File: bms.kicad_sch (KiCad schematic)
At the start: 101 parts, among them J1 CELL_TAPS, J2 SWD, J3 I2C_IN, J4 I2C_OUT, SW1 SW_Push, U1 LMR51610, U2 STM32F103C8Tx, U3 MAX14920, U4 MAX11163, U5 MAX6126, U6 ADuM1252, Y1 8M

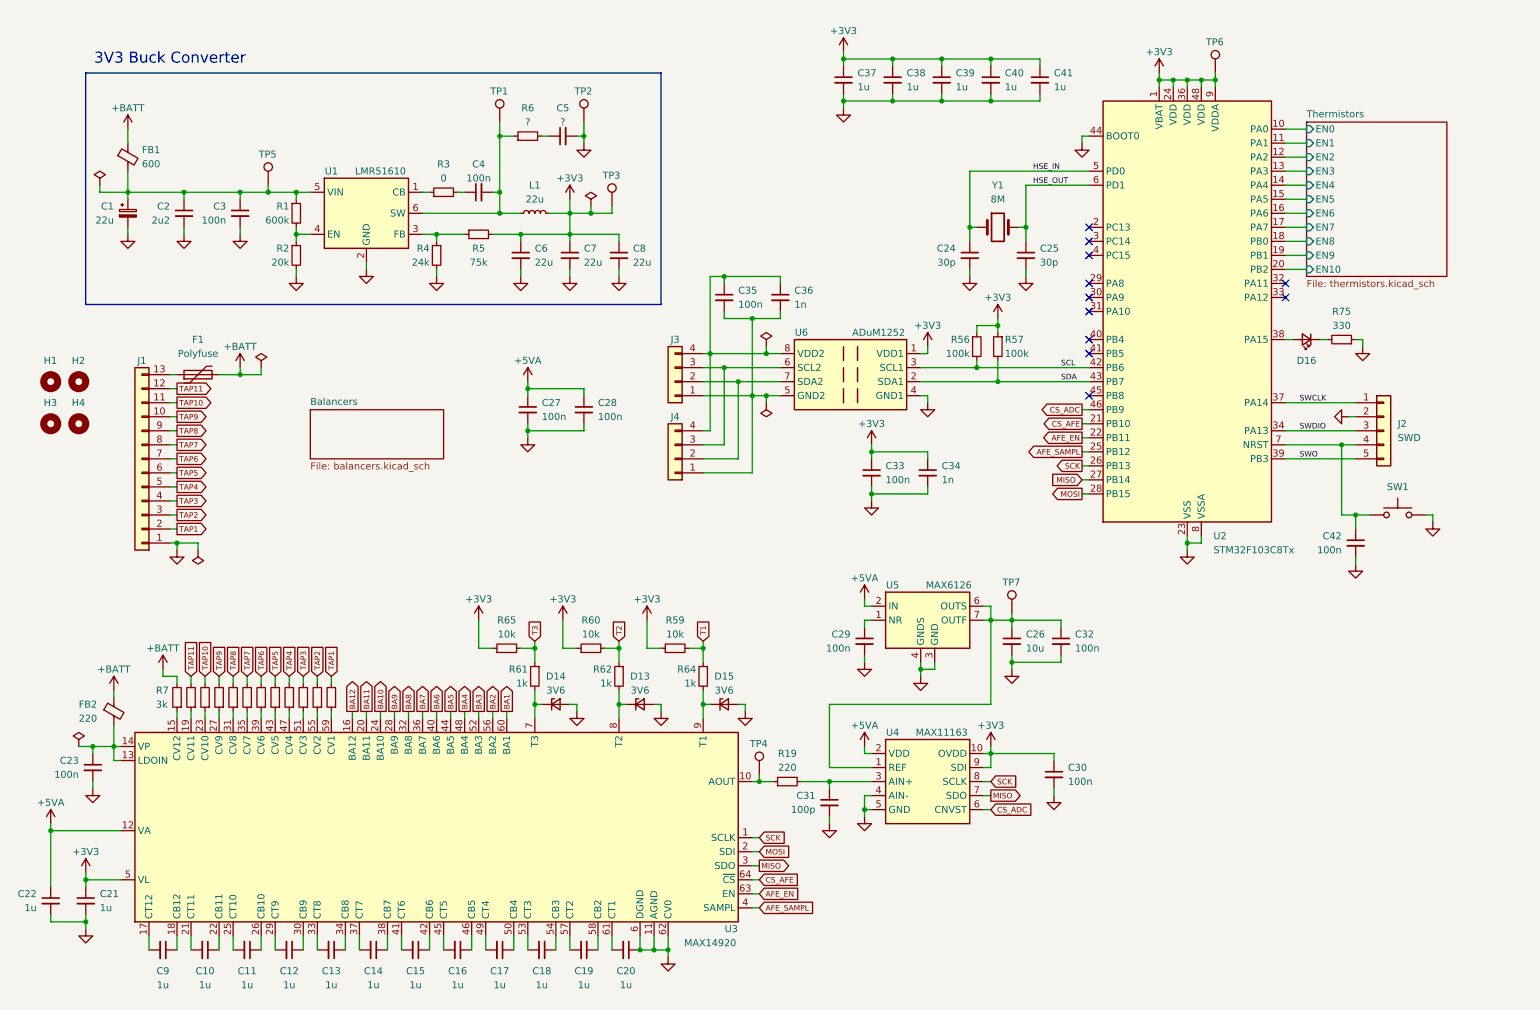
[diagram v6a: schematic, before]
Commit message: schematic: Cleanup
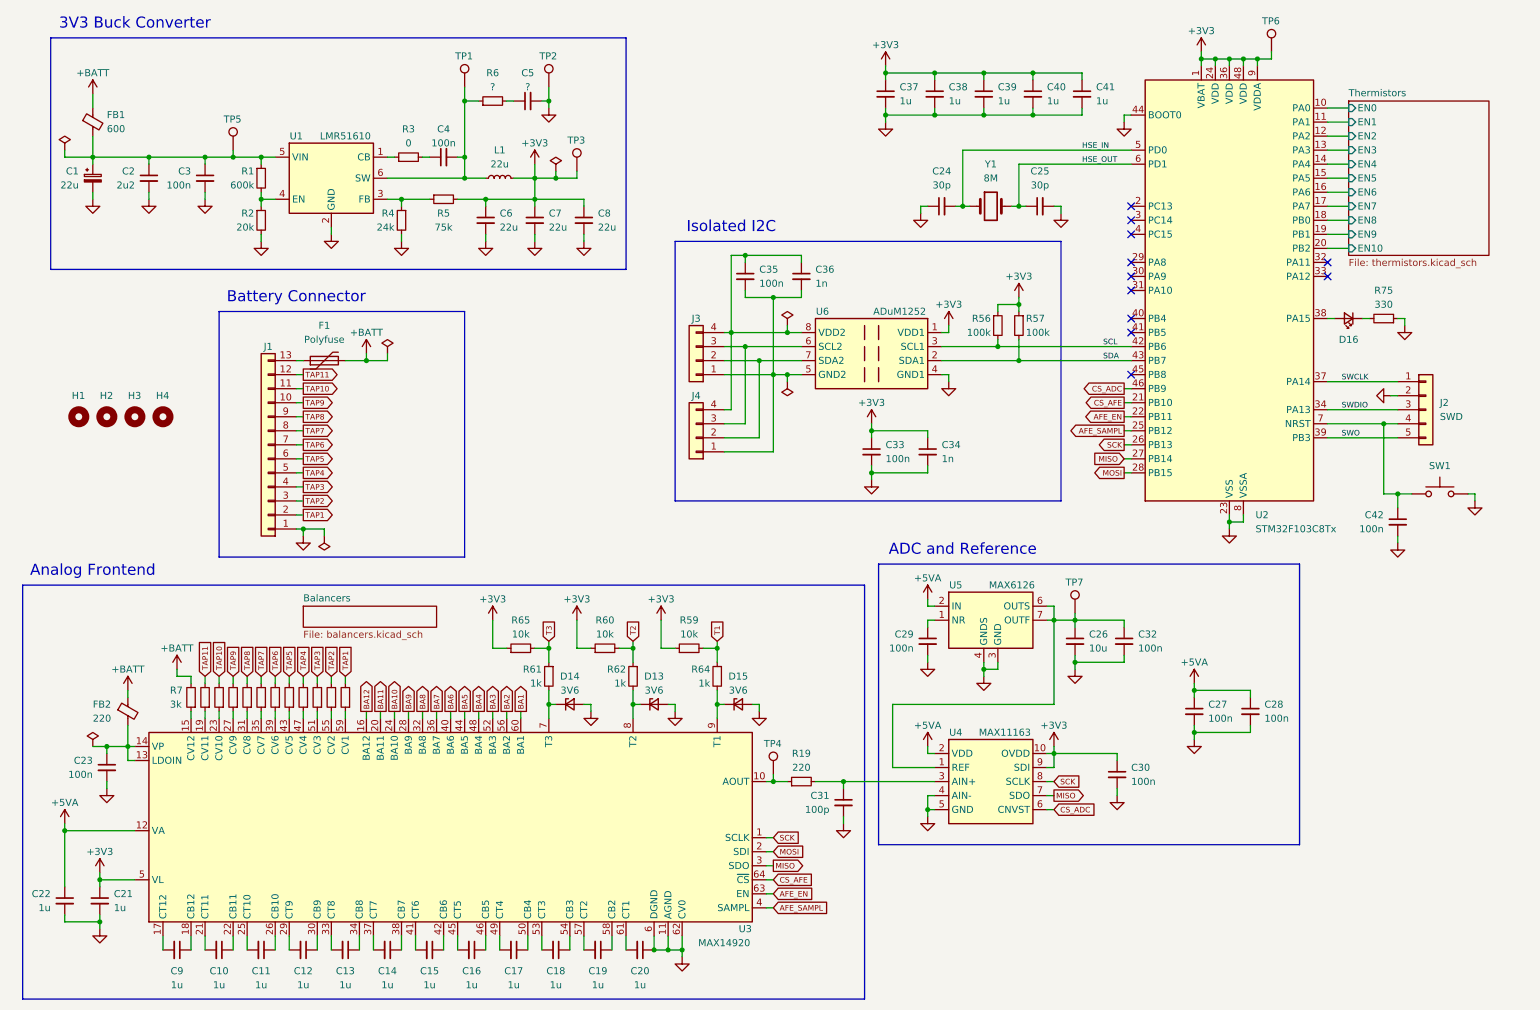
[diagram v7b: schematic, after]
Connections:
- net GND: now also C24.1; no longer C24.2
- net HSE_IN: now also C24.2; no longer C24.1
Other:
- note added: "ADC and Reference"
- note added: "Analog Frontend"
- note added: "Battery Connector"
- note added: "Isolated I2C"
- moved on the sheet: C1, C10, C11, C12, C13, C14, C15, C16, C17, C18, C19, C2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

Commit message: schematic: Re-annotate designators
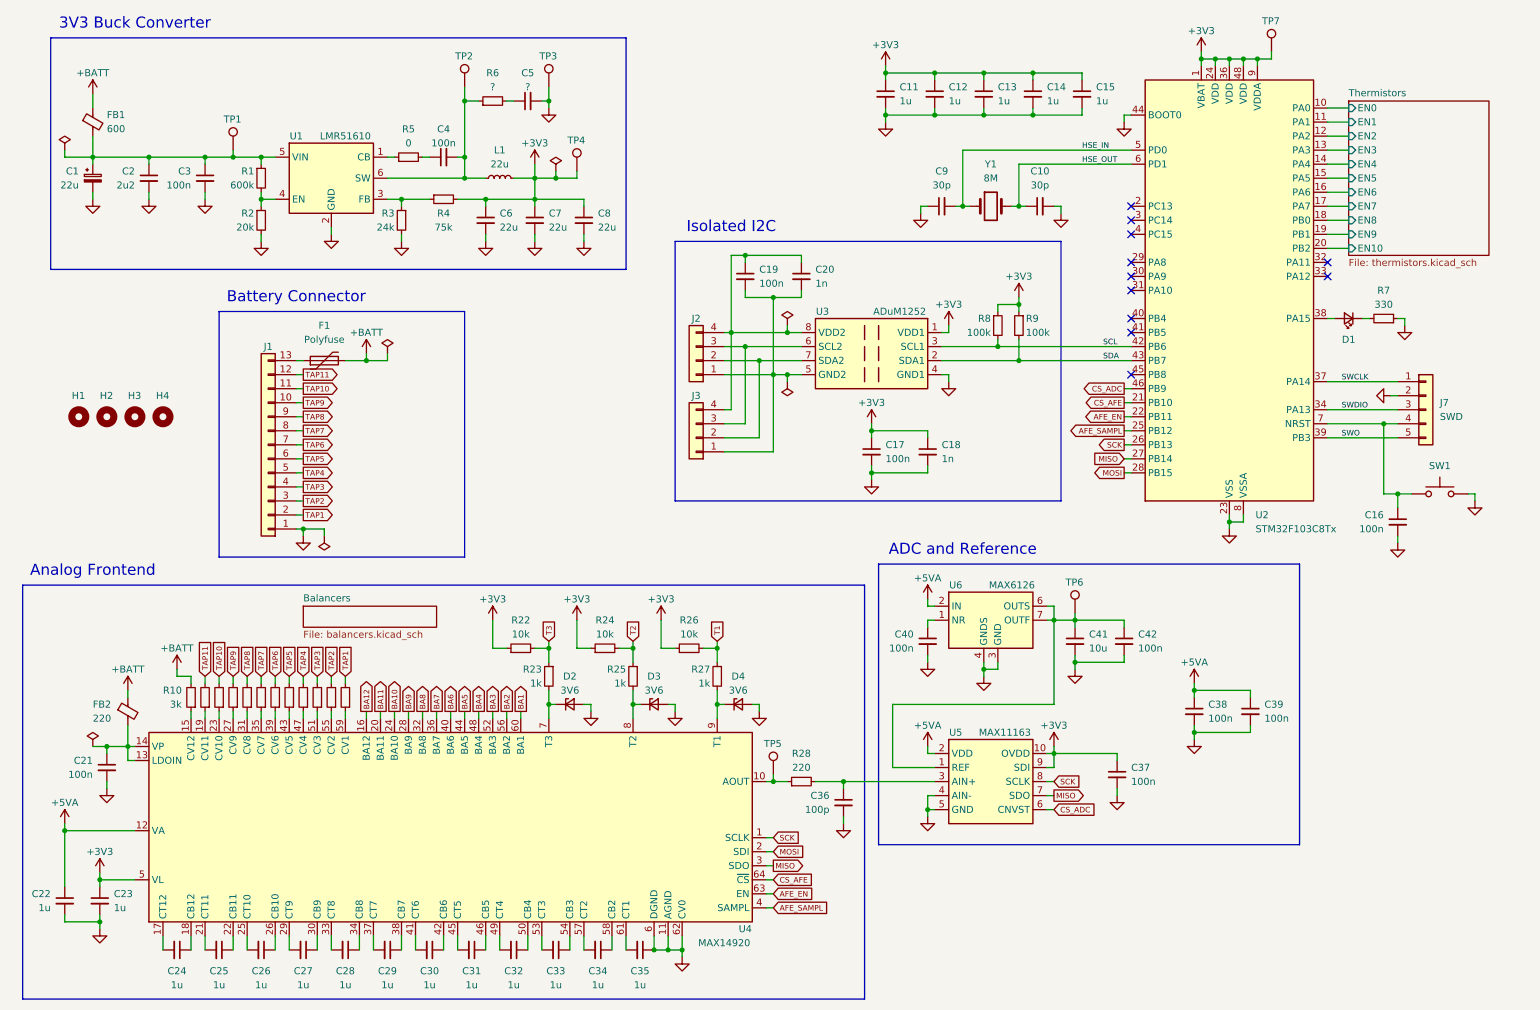
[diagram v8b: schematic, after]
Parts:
- C10: renamed from C25; Role Crystal load capacitor -> MCU crystal load capacitor
- C11: renamed from C37; Role (none) -> MCU decoupling
- C12: renamed from C38; Role (none) -> MCU decoupling
- C13: renamed from C39; Role (none) -> MCU decoupling
- C14: renamed from C40; Role (none) -> MCU decoupling
- C15: renamed from C41; Role (none) -> MCU decoupling
- C16: renamed from C42; Role (none) -> MCU reset button debounce
- C17: renamed from C33; Role AduM1252 side 1 decoupling -> AduM1252 local side decoupling
- C18: renamed from C34; Role AduM1252 side 1 decoupling -> AduM1252 local side decoupling
- C19: renamed from C35; Role AduM1252 side 2 decoupling -> AduM1252 bus side decoupling
- C20: renamed from C36; Role AduM1252 side 2 decoupling -> AduM1252 bus side decoupling
- C21: renamed from C23; Role MAX14920 Vin local decoupling -> MAX14920 Vp and LDOIN decoupling
- C22: Role MAX14920 Vanalog local decoupling -> MAX14920 Va output decoupling
- C23: renamed from C21; Role MAX14920 Vlogic local decoupling -> MAX14920 Vl decoupling
- C36: renamed from C31; Role MAX14920 AOUT filtering -> MAX14920 AOUT filtering capacitor
- C37: renamed from C30; Role MAX11163 local decoupling -> MAX11163 logic decoupling
- C38: renamed from C27; Role MAX11163 local decoupling -> MAX11163 analog decoupling
- C39: renamed from C28; Role MAX6126 local decoupling -> MAX6126 analog decoupling
- C41: renamed from C26; Role MAX6126 output reference decoupling -> MAX6126 output decoupling
- C42: renamed from C32; Role MAX6126 output reference decoupling -> MAX6126 output decoupling
- C9: renamed from C24; Role Crystal load capacitor -> MCU crystal load capacitor
- J2: renamed from J3; Role (none) -> I2C connector
- J3: renamed from J4; Role (none) -> I2C connector
- R28: renamed from R19; Role MAX14920 AOUT filtering -> MAX14920 AOUT filtering resistor
- renumbered C9 to C24, C10 to C25, C11 to C26, C12 to C27, C13 to C28, C14 to C29, C15 to C30, C16 to C31, C17 to C32, C18 to C33, C19 to C34, C20 to C35, C29 to C40, D16 to D1, D14 to D2, D13 to D3, D15 to D4, J2 to J7, R7 to R10, R8 to R11, R9 to R12, R10 to R13, R11 to R14, R12 to R15, R13 to R16, R14 to R17, R15 to R18, R16 to R19, R17 to R20, R18 to R21, R65 to R22, R61 to R23, R60 to R24, R62 to R25, R59 to R26, R64 to R27, R4 to R3, R5 to R4, R3 to R5, R75 to R7, R56 to R8, R57 to R9, TP5 to TP1, TP1 to TP2, TP2 to TP3, TP3 to TP4, TP4 to TP5, TP7 to TP6, TP6 to TP7, U6 to U3, U3 to U4, U4 to U5, U5 to U6
